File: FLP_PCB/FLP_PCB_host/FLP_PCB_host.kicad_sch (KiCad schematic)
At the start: 91 parts, among them J3 GRPB052VWVN-RC, J4 OLED, J5 SMA-J-P-X-ST-TH1, Q1 Q_PMOS_DSG, Q2 UMH3N, U1 ESP32-WROOM-32E, U2 TPS61200DRC, U3 MCP73831-2-OT, U4 AMS1117-3.3, U5 CP2104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

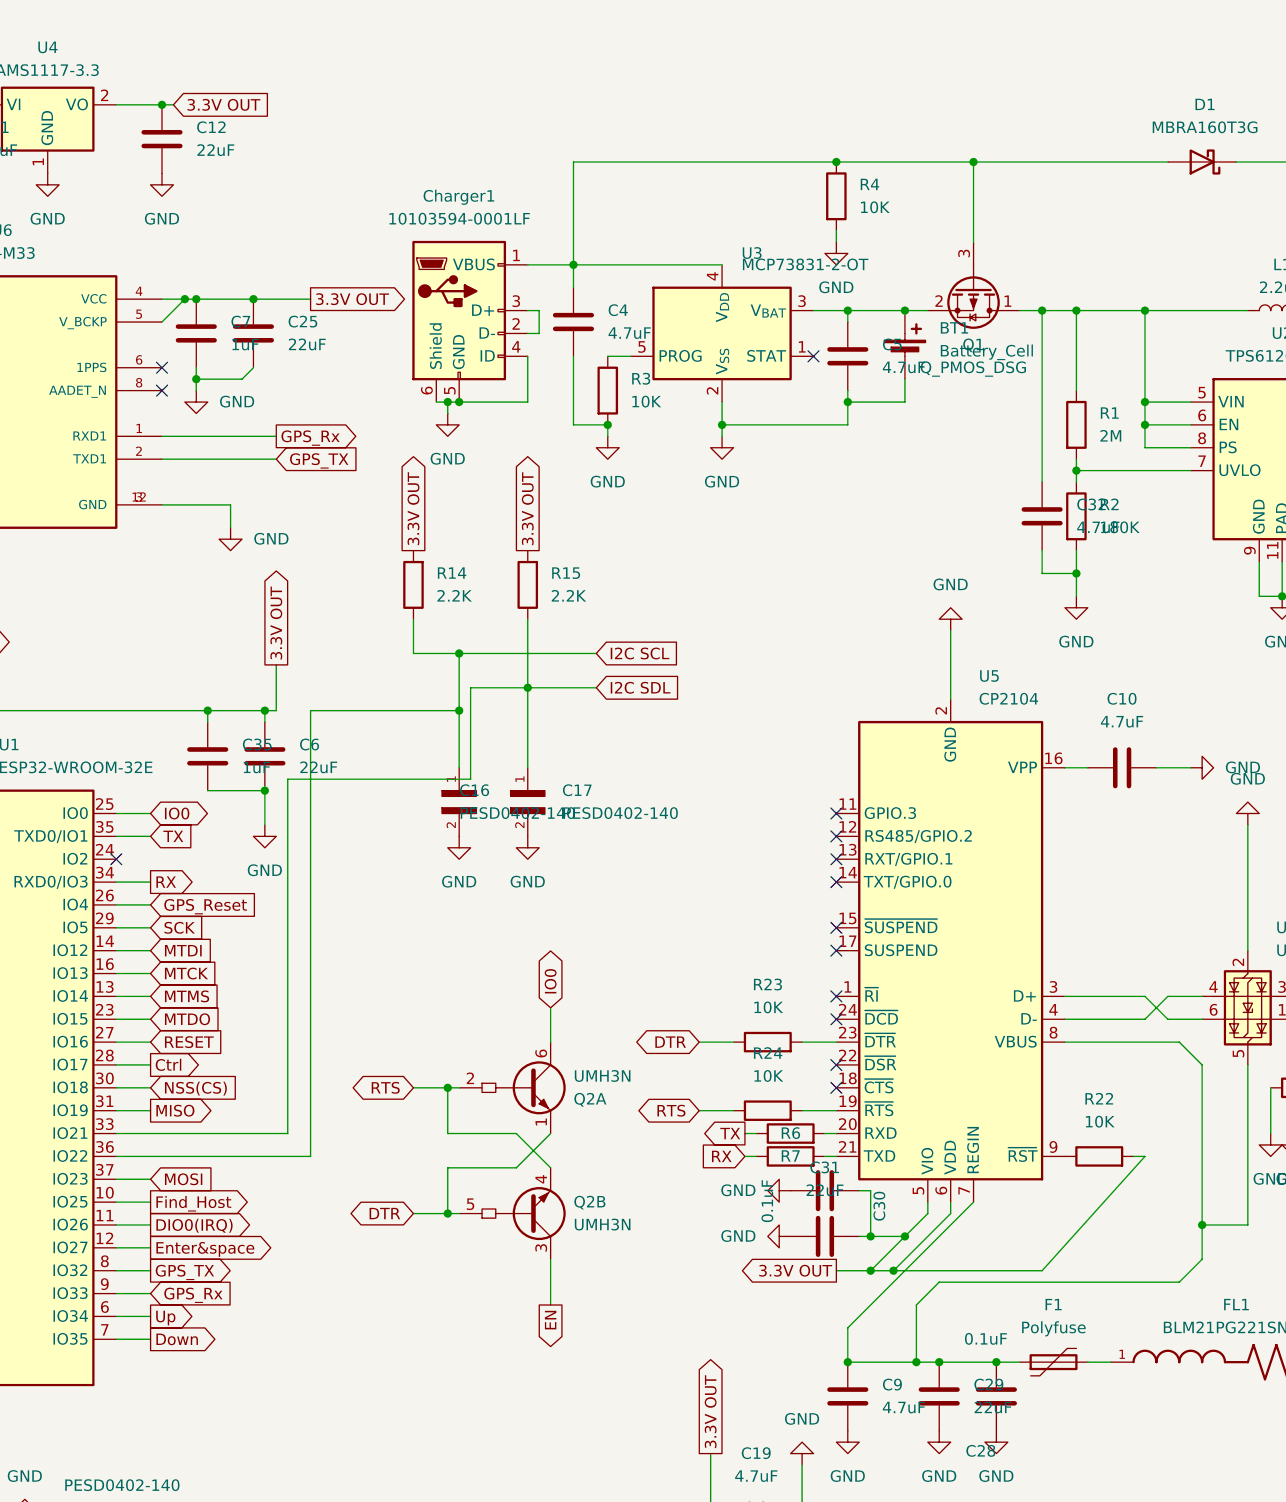
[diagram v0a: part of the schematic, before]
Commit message: dir name change, host PCB finish
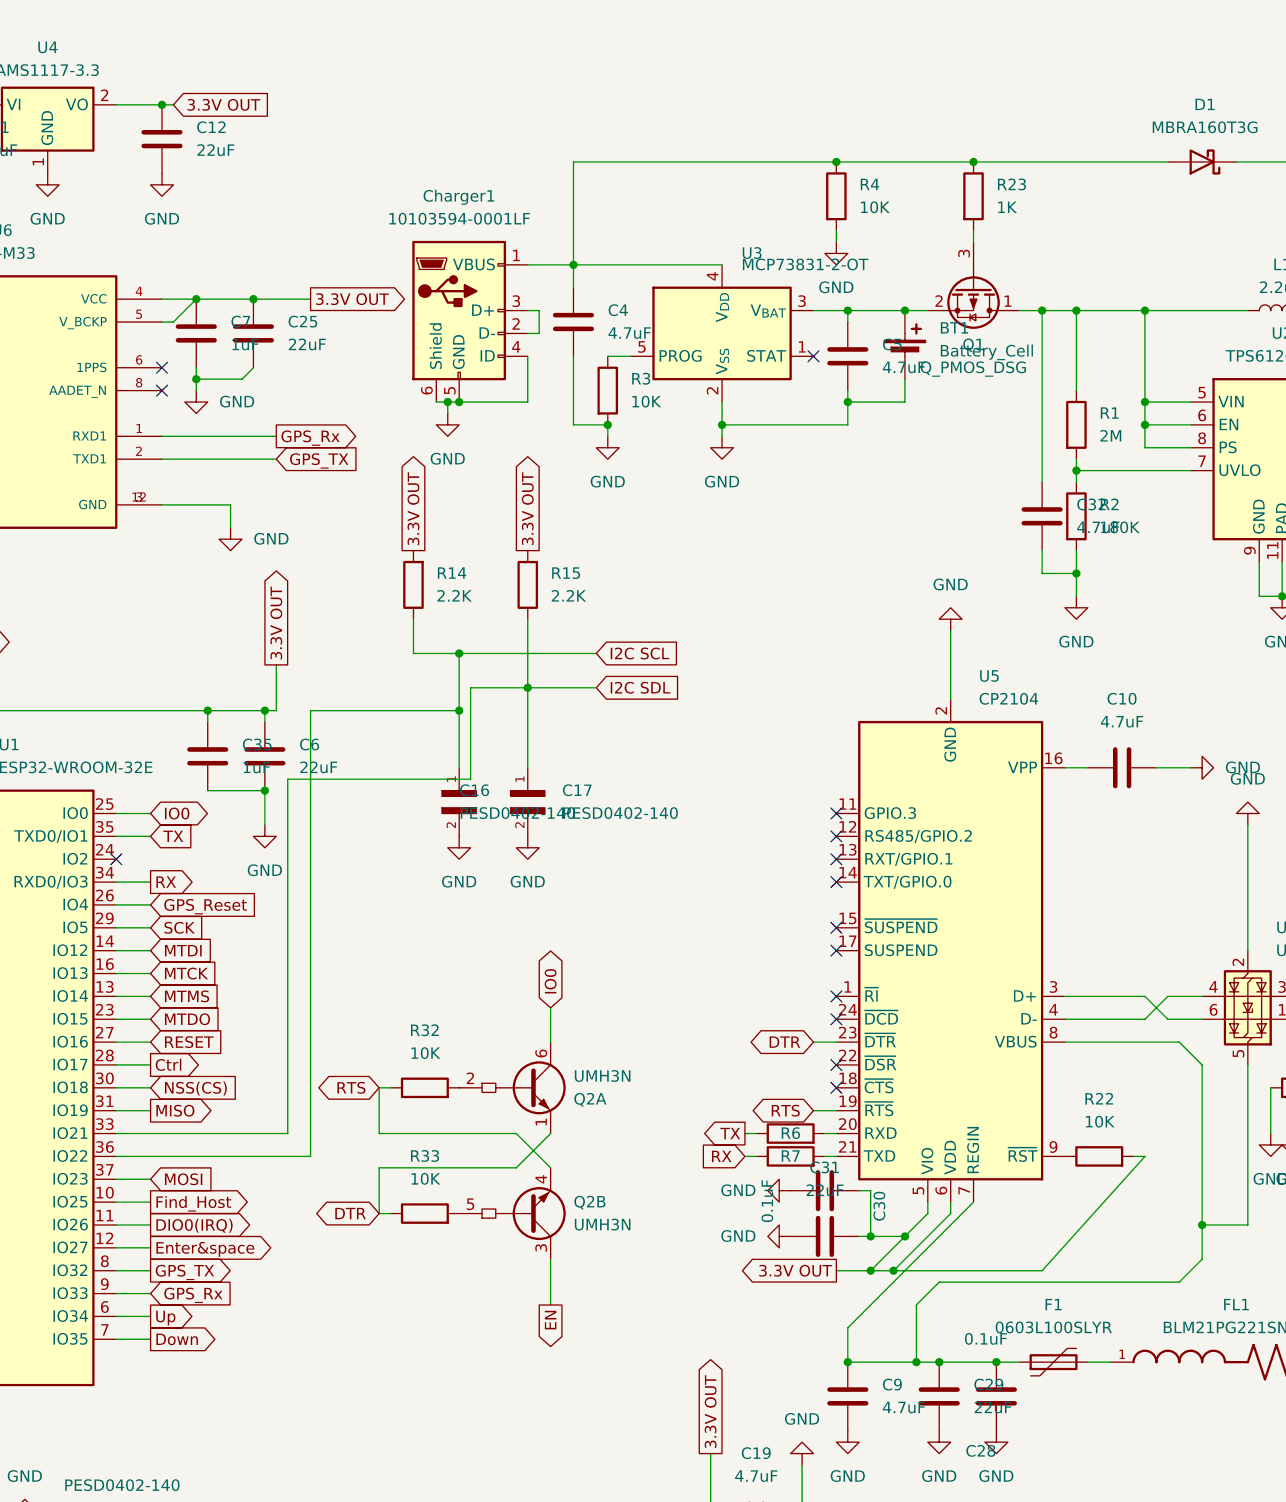
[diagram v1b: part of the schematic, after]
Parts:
- removed R24: 10K, Resistor_SMD:R_0603_1608Metric, symbol Device:R
- added R32, R33: 10K, Resistor_SMD:R_0603_1608Metric, symbol Device:R
- F1: value Polyfuse -> 0603L100SLYR
- R23: value 10K -> 1K
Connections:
- net DTR: now also U5.23 (~{DTR}), R33.1; no longer Q2.5 (B2), R23.1
- net RTS: now also U5.19 (~{RTS}), R32.1; no longer Q2.2 (B1)
- net at R23.2: now also Q1.3 (G); no longer U5.23 (~{DTR})
- net at C4.1, Charger1.1 (VBUS), D1.2 (A)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: now also R23.1; no longer Q1.3 (G)
- new net: Q2.2 (B1), R32.2
- new net: Q2.5 (B2), R33.2

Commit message: modify
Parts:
- Y1: footprint Crystal:Crystal_SMD_2012-2Pin_2.0x1.2mm -> Crystal:Crystal_SMD_2016-4Pin_2.0x1.6mm
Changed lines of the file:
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@@
 			)
 		)
-		(property "Footprint" "Crystal:Crystal_SMD_2012-2Pin_2.0x1.2mm"
+		(property "Footprint" "Crystal:Crystal_SMD_2016-4Pin_2.0x1.6mm"
 			(at 237.49 74.93 0)
 			(effects

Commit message: code adding
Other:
- moved on the sheet: C20, J5, L4
